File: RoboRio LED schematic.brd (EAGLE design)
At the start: 18.7 x 74.9 mm, 50 parts

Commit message: Added labels and removed component names from board.
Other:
- board size 18.7 x 74.9 mm -> 18.7 x 80 mm
- board text added: "+"
- board text added: "GND"
- board text added: "Hgih"
- board text added: "Low"
- board text added: "Sig"

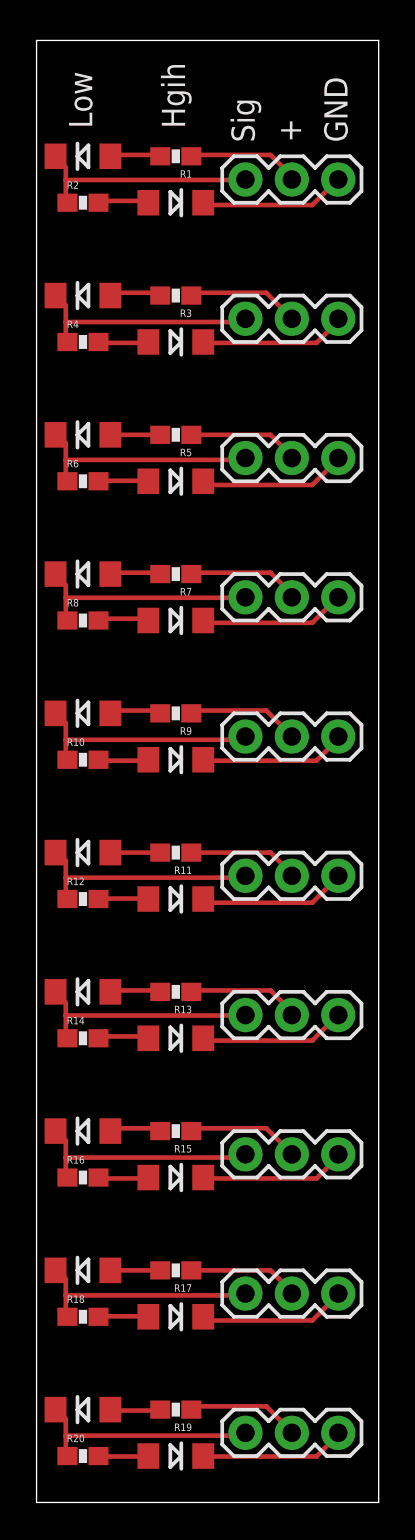
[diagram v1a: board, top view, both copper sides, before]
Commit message: Routed the through hold board. Change LED component to indicate true component size
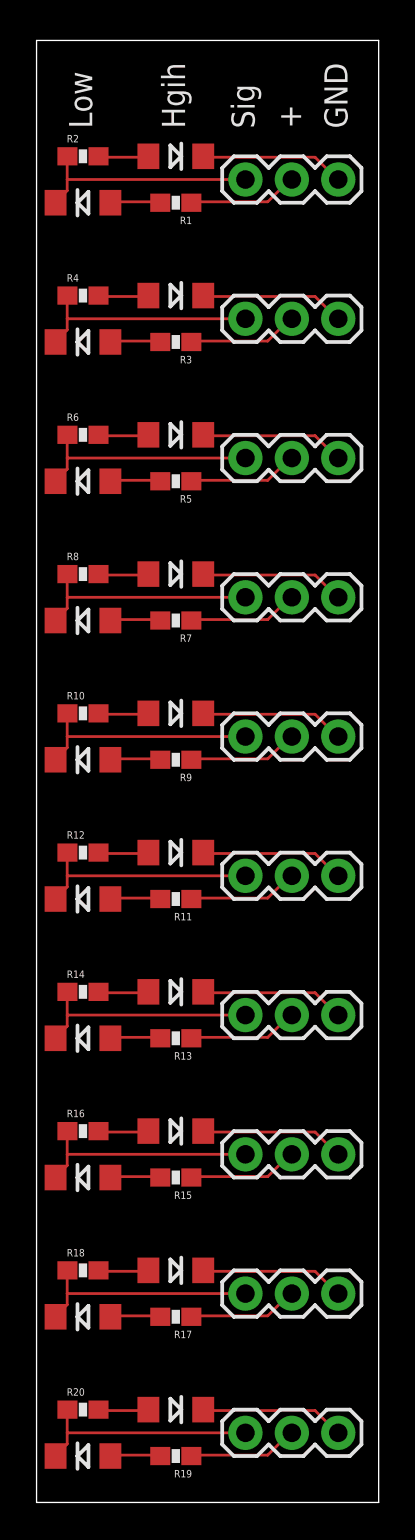
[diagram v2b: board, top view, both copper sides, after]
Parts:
- moved D3 2.54 mm to (2.54, 63.5)
- moved D4 2.54 mm to (7.62, 66.0)
- moved R3 2.54 mm to (7.62, 63.5)
- moved R4 2.54 mm to (2.54, 66.0)
- moved D13 2.54 mm to (2.54, 25.4)
- moved D14 2.54 mm to (7.62, 27.9)
- moved R13 2.54 mm to (7.62, 25.4)
- moved R14 2.54 mm to (2.54, 27.9)
- moved D19 2.54 mm to (2.54, 2.54)
- moved D20 2.54 mm to (7.62, 5.08)
- moved R19 2.54 mm to (7.62, 2.54)
- moved R20 2.54 mm to (2.54, 5.08)
- moved D10 2.54 mm to (7.62, 43.2)
- moved D11 2.54 mm to (2.54, 33.0)
- moved D12 2.54 mm to (7.62, 35.6)
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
